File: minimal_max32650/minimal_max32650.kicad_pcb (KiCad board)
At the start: 4 copper layers, 45.2 x 34.3 mm, 38 parts, among them J1 FTSH-105-01-L-DV-K, U1 MAX32650GCE+, U2 ADP225ACPZ-R7

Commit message: development backup
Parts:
- added C28: 4.7 µF, capacitor_footprints:C_0603_1608Metric, F.Cu at (181.7, 75.6)
- added C29: 0.1uF, capacitor_footprints:C_0402_1005Metric, F.Cu at (182.0, 77.0)
- added C30: 1 µF, capacitor_footprints:C_0402_1005Metric, F.Cu at (178.7, 77.0)
- added TP5: TestPoint, test_point_footprints:TestPoint_THTPad_Castelated, F.Cu at (191.0, 73.3)
- added TP6: TestPoint, test_point_footprints:TestPoint_THTPad_Castelated, F.Cu at (189.7, 73.3)
- added U3: MAXQ1065GTC+, analog_devices_footprints:21-0664_TD1233&plus_1C_MXM, F.Cu at (181.0, 79.8)
- moved C26 7.74 mm to (192.9, 78.8)
- moved TP3 7.63 mm to (195.0, 77.7)
- moved TP4 7.63 mm to (195.0, 80.2)
- moved C25 7.43 mm to (190.4, 79.1), turned to 180 degrees
- moved R1 7.25 mm to (188.4, 81.9)
- moved R3 7.25 mm to (192.3, 81.9)
- moved R2 7.25 mm to (188.4, 83.8)
- moved R4 7.25 mm to (192.3, 83.8)
- moved U2 7.25 mm to (190.4, 82.8)
- moved TP1 6.87 mm to (185.8, 77.7)
- moved TP2 6.87 mm to (185.8, 80.2)
- moved C24 6.72 mm to (187.9, 78.8)
- renumbered C26 to C24, C24 to C25, C25 to C26, R2 to R1, R4 to R2, R1 to R3, R3 to R4, TP4 to TP3, TP3 to TP4
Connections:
- U1 pad 1: unconnected-(U1-P2.16-Pad1) -> /MAXQ1065_RDY
- U1 pad 10: unconnected-(U1-P0.22-Pad10) -> /SPI0_SS0
- U1 pad 138: unconnected-(U1-P3.1-Pad138) -> /SPI0_MISO
- U1 pad 141: unconnected-(U1-P3.2-Pad141) -> /SPI0_MOSI
- U1 pad 142: unconnected-(U1-P3.3-Pad142) -> /SPI0_SCK
- U1 pad 2: unconnected-(U1-P0.1-Pad2) -> /MAXQ1065_WDI
- U1 pad 3: unconnected-(U1-P0.2-Pad3) -> /MAXQ1065_PDWN
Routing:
- net /MAXQ1065_PDWN: track 0.00 -> 15.5 mm, vias 0 -> 2
- net /MAXQ1065_WDI: track 0.00 -> 12.9 mm, vias 0 -> 2
- net /MAXQ1065_RDY: track 0.00 -> 11.3 mm, vias 0 -> 2
- net /SPI0_SS0: track 0.00 -> 11.0 mm, vias 0 -> 2
- net /SPI0_MISO: track 0.00 -> 8.00 mm, vias 0 -> 2
- net /SPI0_MOSI: track 0.00 -> 7.77 mm, vias 0 -> 2
- net /SPI0_SCK: track 0.00 -> 6.40 mm, vias 0 -> 2
- net /3V3: track 25.4 -> 30.0 mm, vias 13 -> 15
- net Net-(U3-CEXT): track 0.00 -> 2.42 mm
- net unconnected-(U1-P2.15-Pad144): track 0.00 -> 1.27 mm, vias 0 -> 1
- net unconnected-(U1-P2.14-Pad143): track 0.00 -> 1.27 mm, vias 0 -> 1
- net GND: vias 35 -> 39
- added copper zone on In1.Cu, net /3V3
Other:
- board size 45.2 x 34.3 mm -> 50.3 x 34.3 mm

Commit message: development backup
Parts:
- added C5: 0.1uF, capacitor_footprints:C_0402_1005Metric, F.Cu at (152.3, 84.9)
- added D1: 1.8 V, diode_footprints:LED_GREEN_0402_1005Metric, F.Cu at (179.0, 85.1)
- added D2: 1.8 V, diode_footprints:LED_GREEN_0402_1005Metric, F.Cu at (183.9, 85.1)
- added Q1: 50 V, transistor_footprints:SOT23-3, F.Cu at (181.3, 85.6)
- added Q2: 50 V, transistor_footprints:SOT23-3, F.Cu at (186.2, 85.6)
- added R1: 10k, resistor_footprints:R_0402_1005Metric, F.Cu at (151.0, 76.1)
- added R2: 10k, resistor_footprints:R_0402_1005Metric, F.Cu at (152.2, 76.1)
- added R3: 10k, resistor_footprints:R_0402_1005Metric, F.Cu at (153.4, 76.1)
- added R4: 1 kΩ, resistor_footprints:R_0402_1005Metric, F.Cu at (179.5, 83.4)
- added R5: 1 kΩ, resistor_footprints:R_0402_1005Metric, F.Cu at (184.4, 83.4)
- added U1: ADT75BRMZ, analog_devices_footprints:RM_8_ADI, F.Cu at (151.8, 81.0)
- moved TP5 10.4 mm to (197.9, 79.7), turned to 180 degrees
- moved TP6 10.3 mm to (197.9, 80.9), turned to 180 degrees
- moved TP3 8.00 mm to (193.5, 75.7), turned to 180 degrees
- moved TP4 7.40 mm to (193.5, 84.9), turned to 180 degrees
- moved TP1 6.89 mm to (191.0, 75.7), turned to 180 degrees
- moved TP2 6.18 mm to (191.0, 84.9), turned to 180 degrees
- moved R6 5.59 mm to (187.4, 78.3), turned to 180 degrees
- moved R7 5.23 mm to (187.4, 82.3), turned to 180 degrees
- moved C30 4.59 mm to (192.4, 77.8), turned to 0 degrees
- moved C31 4.01 mm to (192.4, 82.8), turned to 0 degrees
- moved R8 3.63 mm to (189.3, 78.3), turned to 180 degrees
- moved U4 3.17 mm to (188.4, 80.3), turned to 0 degrees
- moved R9 3.04 mm to (189.3, 82.3), turned to 180 degrees
- moved C29 2.04 mm to (192.0, 80.3), turned to 90 degrees
- moved C28 1.48 mm to (190.7, 89.6)
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- renumbered C9 to C10, C10 to C11, C11 to C12, C12 to C13, C13 to C14, C14 to C15, C15 to C16, C16 to C17, C17 to C18, C18 to C19, C30 to C20, C19 to C21, C20 to C22, C21 to C23, C22 to C24, C23 to C25, C28 to C26, C29 to C27, C27 to C28, C25 to C29, C24 to C30, C26 to C31, C5 to C6, C6 to C7, C7 to C8, C8 to C9, R2 to R6, R4 to R7, R1 to R8, R3 to R9, TP2 to TP1, TP4 to TP2, TP1 to TP3, TP3 to TP4, TP6 to TP5, TP5 to TP6, U1 to U2, U2 to U4
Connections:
- U2 pad 143: unconnected-(U1-P2.14-Pad143) -> /LED2
- U2 pad 144: unconnected-(U1-P2.15-Pad144) -> /LED1
- U2 pad 19: unconnected-(U1-P2.17-Pad19) -> /I2C1_SDA
- U2 pad 20: unconnected-(U1-P2.18-Pad20) -> /I2C1_SCL
- U2 pad 39: unconnected-(U1-P1.1-Pad39) -> /ADT75_OS/ALERT
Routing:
- net /I2C1_SCL: track 0.00 -> 17.7 mm, vias 0 -> 2
- net /TCK: track 0.00 -> 16.7 mm, vias 0 -> 2
- net /I2C1_SDA: track 0.00 -> 16.6 mm, vias 0 -> 2
- net /TMS: track 0.00 -> 15.6 mm, vias 0 -> 2
- net /LED1: track 0.00 -> 13.7 mm
- net /UART0_TX: track 0.00 -> 12.5 mm, vias 0 -> 2
- net /RSTN: track 0.00 -> 11.3 mm, vias 0 -> 2
- net /UART0_RX: track 0.00 -> 10.9 mm, vias 0 -> 2
- net /ADT75_OS/ALERT: track 0.00 -> 9.95 mm, vias 0 -> 2
- net /LED2: track 0.00 -> 8.69 mm
- net /3V3: track 30.0 -> 36.3 mm, vias 15 -> 21
- net Net-(D4-Pad2): track 0.00 -> 1.32 mm
- net Net-(D3-Pad2): track 0.00 -> 1.32 mm
- net Net-(Q3-D): track 0.00 -> 1.30 mm
- net Net-(Q2-D): track 0.00 -> 1.30 mm
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- added copper zone on B.Cu, net /1V1
- added copper zone on In1.Cu, net /1V8

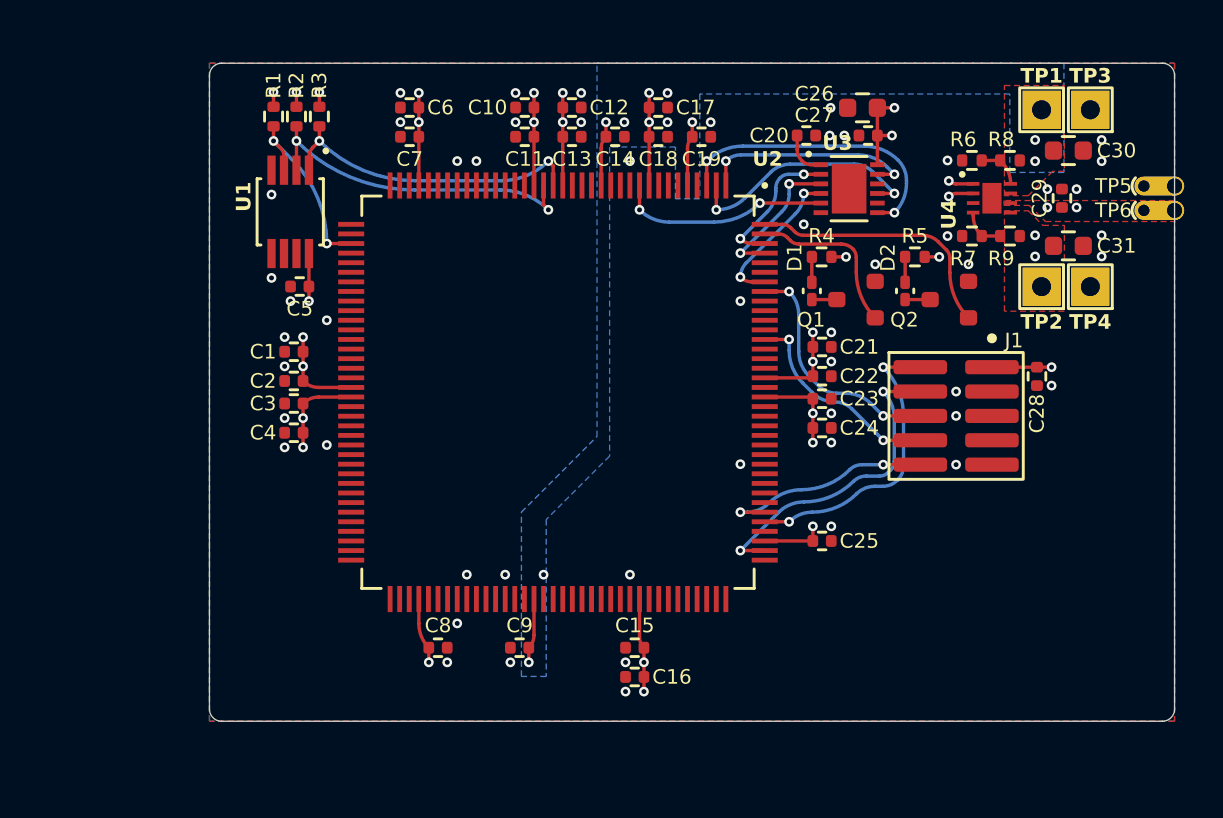
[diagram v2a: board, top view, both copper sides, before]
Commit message: Add SPI interface color mappings to KiCad project
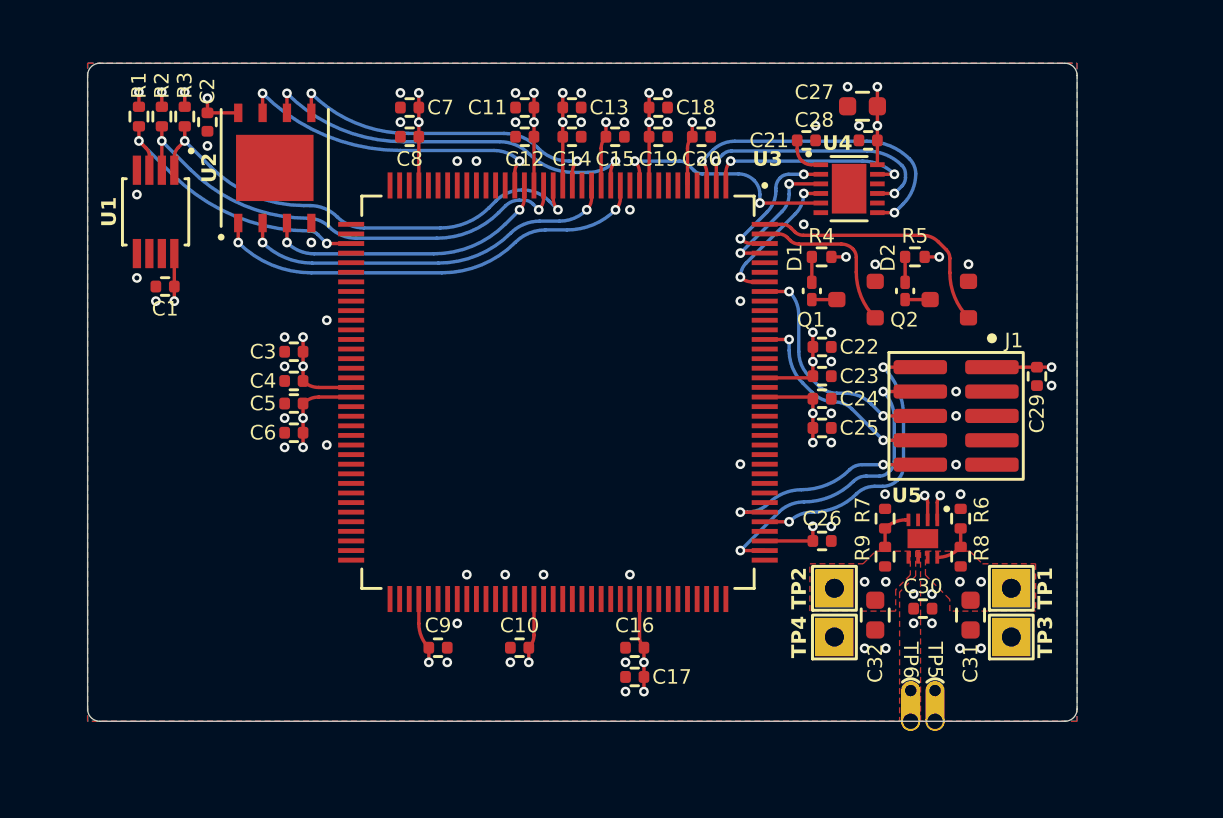
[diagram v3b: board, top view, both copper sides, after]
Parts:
- added C2: 100 nF, capacitor_footprints:C_0402_1005Metric, F.Cu at (147.5, 76.3)
- added U2: MX25U6432FZNI02, macronix_footprints:WSON-8_6X5_MAC, F.Cu at (151.0, 78.7)
- C1: renamed from C5; value 0.1uF -> 100 nF
- C28: renamed from C27; value 0.1uF -> 100 nF
- C29: renamed from C28; value 0.1uF -> 100 nF
- moved TP5 30.6 mm to (185.4, 107.6), turned to 90 degrees
- moved TP6 30.0 mm to (184.2, 107.6), turned to 90 degrees
- moved TP3 27.8 mm to (189.4, 103.2), turned to 90 degrees
- moved TP1 25.0 mm to (189.4, 100.6), turned to 90 degrees
- moved C31 24.7 mm to (187.3, 102.0), turned to -90 degrees
- moved TP4 22.6 mm to (180.2, 103.2), turned to 90 degrees
- moved C30 22.6 mm to (184.8, 101.7), turned to 0 degrees
- moved C32 21.7 mm to (182.3, 102.0), turned to -90 degrees
- moved R8 20.8 mm to (186.8, 99.0), turned to 90 degrees
- moved TP2 19.1 mm to (180.2, 100.6), turned to 90 degrees
- moved R6 18.7 mm to (186.8, 97.0), turned to 90 degrees
- moved U5 18.1 mm to (184.8, 98.1), turned to -90 degrees
- moved R9 17.9 mm to (182.8, 99.0), turned to 90 degrees
- moved R7 15.4 mm to (182.8, 97.0), turned to 90 degrees
- moved C1 7.02 mm to (145.3, 84.9)
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- renumbered C9 to C10, C10 to C11, C11 to C12, C12 to C13, C13 to C14, C14 to C15, C15 to C16, C16 to C17, C17 to C18, C18 to C19, C19 to C20, C20 to C21, C21 to C22, C22 to C23, C23 to C24, C24 to C25, C25 to C26, C26 to C27, C1 to C3, C29 to C30, C30 to C31, C31 to C32, C2 to C4, C3 to C5, C4 to C6, C6 to C7, C7 to C8, C8 to C9, U2 to U3, U3 to U4, U4 to U5
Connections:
- U3 pad 12: unconnected-(U1-P0.7-Pad12) -> /SPIXF_SS0
- U3 pad 13: unconnected-(U1-P0.8-Pad13) -> /SPIXF_SCK
- U3 pad 15: unconnected-(U1-P0.9-Pad15) -> /SPIXF_SDIO1
- U3 pad 17: unconnected-(U1-P0.10-Pad17) -> /SPIXF_SDIO0
- U3 pad 22: unconnected-(U1-P0.11-Pad22) -> /SPIXF_SDIO2
- U3 pad 23: unconnected-(U1-P0.12-Pad23) -> /SPIXF_SDIO3
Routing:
- net /SPIXF_SS0: track 0.00 -> 23.3 mm, vias 0 -> 2
- net /SPIXF_SCK: track 0.00 -> 20.6 mm, vias 0 -> 2
- net /SPIXF_SDIO1: track 0.00 -> 20.2 mm, vias 0 -> 2
- net /SPIXF_SDIO0: track 0.00 -> 17.1 mm, vias 0 -> 2
- net /SPIXF_SDIO3: track 0.00 -> 16.6 mm, vias 0 -> 2
- net /SPIXF_SDIO2: track 0.00 -> 15.3 mm, vias 0 -> 2
- net /I2C1_SDA: track 16.6 -> 25.5 mm
- net /I2C1_SCL: track 17.7 -> 25.5 mm
- net /ADT75_OS/ALERT: track 9.95 -> 15.2 mm
- net /1V8: track 30.6 -> 33.0 mm, vias 14 -> 15
- net /MAXQ1065_PDWN: track 15.5 -> 16.9 mm
- net /SPI0_SS0: track 11.1 -> 12.3 mm
- net /MAXQ1065_WDI: track 13.0 -> 13.9 mm
- net /3V3: track 36.3 -> 35.8 mm
- net GND: vias 56 -> 58
- removed copper zone on B.Cu, net /1V1
- removed copper zone on In1.Cu, net /1V8
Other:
- board size 50.3 x 34.3 mm -> 51.6 x 34.3 mm

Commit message: development backup
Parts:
- added C35: 100 nF, capacitor_footprints:C_0402_1005Metric, F.Cu at (142.7, 90.3)
- added C36: 100 nF, capacitor_footprints:C_0402_1005Metric, F.Cu at (144.2, 90.3)
- added C37: 1 µF, capacitor_footprints:C_0402_1005Metric, F.Cu at (145.7, 90.3)
- added C38: 1 µF, capacitor_footprints:C_0402_1005Metric, F.Cu at (141.4, 95.6)
- added C39: 100 nF, capacitor_footprints:C_0402_1005Metric, F.Cu at (141.4, 94.1)
- added C40: 100 nF, capacitor_footprints:C_0402_1005Metric, F.Cu at (141.4, 92.5)
- added U6: S80KS5122GABHM020, infineon_footprints:PG-BGA-24-801, F.Cu at (146.7, 94.6)
- moved D1 3.43 mm to (182.4, 85.1)
- moved D2 3.43 mm to (187.3, 85.1)
- moved Q1 3.43 mm to (184.7, 85.6)
- moved Q2 3.43 mm to (189.6, 85.6)
- moved R4 3.43 mm to (183.0, 83.4)
- moved R5 3.43 mm to (187.8, 83.4)
- moved R1 1.44 mm to (142.5, 76.1)
- moved R2 1.44 mm to (143.7, 76.1)
- moved R3 1.44 mm to (144.9, 76.1)
- moved U1 1.44 mm to (143.4, 81.0)
- moved U2 1.44 mm to (149.6, 78.7)
- moved C1 1.44 mm to (143.9, 84.9)
- moved C2 1.44 mm to (146.1, 76.3)
- moved R8 1.27 mm to (186.8, 100.3)
- moved R9 1.27 mm to (182.8, 100.3)
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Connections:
- U3 pad 44: unconnected-(U2-P3.0-Pad44) -> /CS1__P3.0
- U3 pad 50: unconnected-(U2-P1.10-Pad50) -> /RESET__P1.10
- U3 pad 52: unconnected-(U2-P1.11-Pad52) -> /CS0__P1.11
- U3 pad 53: unconnected-(U2-P1.12-Pad53) -> /D0__P1.12
- U3 pad 56: unconnected-(U2-P1.13-Pad56) -> /D4__P1.13
- U3 pad 58: unconnected-(U2-P1.15-Pad58) -> /D1__P1.15
- U3 pad 59: unconnected-(U2-P1.16-Pad59) -> /D5__P1.16
- U3 pad 62: unconnected-(U2-P1.19-Pad62) -> /D2__P1.19
- U3 pad 63: unconnected-(U2-P1.18-Pad63) -> /D6__P1.18
- U3 pad 64: unconnected-(U2-~{HYP_CLK}-Pad64) -> /CLK_N
- U3 pad 65: unconnected-(U2-HYP_CLK-Pad65) -> /CLK_P
- U3 pad 66: unconnected-(U2-P1.20-Pad66) -> /D3__P1.20
- U3 pad 67: unconnected-(U2-P1.21-Pad67) -> /D7__P1.21
- U3 pad 68: unconnected-(U2-P1.14-Pad68) -> /RWDS__P1.14
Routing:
- net /D1__P1.15: track 0.00 -> 26.8 mm, vias 0 -> 2
- net /RESET__P1.10: track 0.00 -> 26.1 mm, vias 0 -> 2
- net /CS0__P1.11: track 0.00 -> 23.7 mm, vias 0 -> 2
- net /D0__P1.12: track 0.00 -> 22.3 mm, vias 0 -> 2
- net /D4__P1.13: track 0.00 -> 22.2 mm, vias 0 -> 2
- net /RWDS__P1.14: track 0.00 -> 21.3 mm, vias 0 -> 2
- net /D6__P1.18: track 0.00 -> 21.0 mm, vias 0 -> 2
- net /D7__P1.21: track 0.00 -> 19.5 mm, vias 0 -> 2
- net /D2__P1.19: track 0.00 -> 16.6 mm, vias 0 -> 2
- net /D5__P1.16: track 0.00 -> 14.9 mm, vias 0 -> 2
- net /CLK_N: track 0.00 -> 13.7 mm
- net /D3__P1.20: track 0.00 -> 13.7 mm, vias 0 -> 2
- net /CLK_P: track 0.00 -> 13.6 mm
- net /1V8: track 33.0 -> 45.9 mm, vias 15 -> 22
- net /LED2: track 8.69 -> 12.1 mm
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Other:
- board size 51.6 x 34.3 mm -> 54.1 x 36.8 mm

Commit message: development backup
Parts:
- moved TP1 7.27 mm to (186.4, 97.8), turned to 180 degrees
- moved R5 6.91 mm to (180.2, 100.5), turned to 180 degrees
- moved TP2 6.89 mm to (183.8, 97.8), turned to 180 degrees
- moved TP3 6.72 mm to (186.4, 107.1), turned to 180 degrees
- moved R8 6.68 mm to (180.2, 104.4), turned to 180 degrees
- moved TP4 6.32 mm to (183.8, 107.1), turned to 180 degrees
- moved TP5 6.13 mm to (190.3, 108.8)
- moved TP6 6.13 mm to (191.6, 108.8)
- moved U6 4.73 mm to (181.3, 102.5), turned to 0 degrees
- moved R4 4.58 mm to (182.2, 100.5), turned to 180 degrees
- moved R7 4.21 mm to (182.2, 104.4), turned to 180 degrees
- moved C35 3.91 mm to (185.2, 100.0), turned to 0 degrees
- moved C37 3.35 mm to (185.2, 104.9), turned to 0 degrees
- moved C38 3.35 mm to (186.9, 87.8), turned to 180 degrees
- moved C36 0.53 mm to (184.9, 102.5), turned to 90 degrees
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- renumbered C40 to C1, C4 to C10, C5 to C11, C6 to C12, C7 to C13, C8 to C14, C9 to C15, C10 to C16, C11 to C17, C12 to C18, C13 to C19, C39 to C2, C14 to C20, C15 to C21, C16 to C22, C17 to C23, C18 to C24, C19 to C25, C20 to C26, C21 to C27, C22 to C28, C23 to C29, C38 to C3, C24 to C30, C25 to C31, C26 to C32, C27 to C33, C28 to C34, C31 to C35, C30 to C36, C32 to C37, C29 to C38, C35 to C4, C1 to C5, C36 to C6, C37 to C7, C2 to C8, C3 to C9, R8 to R4, R6 to R5, R4 to R6, R9 to R7, R7 to R8, R5 to R9, TP3 to TP1, TP1 to TP2, TP4 to TP3, TP2 to TP4, TP6 to TP5, TP5 to TP6, U6 to U2, U2 to U3, U3 to U4, U4 to U5, U5 to U6
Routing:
- net /CLK_P: track 13.6 -> 31.0 mm
- net /CLK_N: track 13.7 -> 31.0 mm
- net /D3__P1.20: track 13.7 -> 27.9 mm
- net /D5__P1.16: track 14.9 -> 27.9 mm
- net /D2__P1.19: track 16.6 -> 28.1 mm
- net /D7__P1.21: track 19.5 -> 27.9 mm
- net /D6__P1.18: track 21.0 -> 28.0 mm
- net /RWDS__P1.14: track 21.3 -> 27.9 mm
- net /D4__P1.13: track 22.2 -> 28.1 mm
- net /D1__P1.15: track 26.8 -> 32.5 mm
- net /D0__P1.12: track 22.3 -> 27.9 mm
- net /CS0__P1.11: track 23.7 -> 20.2 mm
- net /RESET__P1.10: track 26.1 -> 22.9 mm
- net /1V8: track 45.9 -> 45.0 mm
- net /TMS: track 15.5 -> 16.3 mm
- added copper zone on In1.Cu, net /1V1
- added copper zone on In1.Cu, net /1V8

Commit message: development backup
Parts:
- added TP1: TestPoint, test_point_footprints:TestPoint_THTPad_Castelated, F.Cu at (141.3, 108.8)
- added TP2: TestPoint, test_point_footprints:TestPoint_THTPad_Castelated, F.Cu at (142.5, 108.8)
- added TP3: TestPoint, test_point_footprints:TestPoint_THTPad_Castelated, F.Cu at (143.8, 108.8)
- added TP4: TestPoint, test_point_footprints:TestPoint_THTPad_Castelated, F.Cu at (145.1, 108.8)
- added TP5: TestPoint, test_point_footprints:TestPoint_THTPad_Castelated, F.Cu at (146.4, 108.8)
- renumbered C36 to C35, C35 to C36, R5 to R4, R8 to R5, R4 to R6, R6 to R8, TP5 to TP10, TP6 to TP11, TP2 to TP6, TP4 to TP7, TP1 to TP8, TP3 to TP9
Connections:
- U4 pad 30: unconnected-(U3-P0.16-Pad30) -> Net-(U4-P0.16)
- U4 pad 31: unconnected-(U3-P0.17-Pad31) -> Net-(U4-P0.17)
- U4 pad 32: unconnected-(U3-P0.18-Pad32) -> Net-(U4-P0.18)
- U4 pad 35: unconnected-(U3-P0.20-Pad35) -> Net-(U4-P0.20)
- U4 pad 36: unconnected-(U3-P0.21-Pad36) -> Net-(U4-P0.21)
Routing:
- net Net-(U4-P0.21): track 0.00 -> 41.6 mm, vias 0 -> 1
- net Net-(U4-P0.20): track 0.00 -> 40.9 mm, vias 0 -> 1
- net Net-(U4-P0.18): track 0.00 -> 40.1 mm, vias 0 -> 1
- net Net-(U4-P0.17): track 0.00 -> 39.3 mm, vias 0 -> 1
- net Net-(U4-P0.16): track 0.00 -> 38.7 mm, vias 0 -> 1
- net /I2C1_SDA: track 26.7 -> 29.1 mm
- net /I2C1_SCL: track 26.8 -> 29.1 mm
- net /SPIXF_SDIO1: track 21.6 -> 23.8 mm
- net /SPIXF_SDIO2: track 16.8 -> 18.9 mm
- net /SPIXF_SS0: track 24.7 -> 26.9 mm
- net /SPIXF_SDIO0: track 18.5 -> 19.9 mm
- net unconnected-(U4-P1.25-Pad72): track 0.00 -> 1.33 mm, vias 0 -> 1
- net unconnected-(U4-P1.23-Pad70): track 0.00 -> 1.33 mm, vias 0 -> 1
- net unconnected-(U4-P1.30-Pad71): track 0.00 -> 1.27 mm, vias 0 -> 1
- net /SPIXF_SCK: track 22.1 -> 23.1 mm
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
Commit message: development backup
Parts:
- added TP1: TestPoint, test_point_footprints:TestPoint_THTPad_Castelated, F.Cu at (145.1, 110.1)
- added TP14: TestPoint, test_point_footprints:TestPoint_THTPad_Castelated, F.Cu at (161.6, 110.1)
- added TP15: TestPoint, test_point_footprints:TestPoint_THTPad_Castelated, F.Cu at (162.9, 110.1)
- added TP16: TestPoint, test_point_footprints:TestPoint_THTPad_Castelated, F.Cu at (164.1, 110.1)
- added TP2: TestPoint, test_point_footprints:TestPoint_THTPad_Castelated, F.Cu at (146.4, 110.1)
- added TP3: TestPoint, test_point_footprints:TestPoint_THTPad_Castelated, F.Cu at (147.6, 110.1)
- added TP4: TestPoint, test_point_footprints:TestPoint_THTPad_Castelated, F.Cu at (148.9, 110.1)
- added TP5: TestPoint, test_point_footprints:TestPoint_THTPad_Castelated, F.Cu at (150.2, 110.1)
- added TP6: TestPoint, test_point_footprints:TestPoint_THTPad_Castelated, F.Cu at (151.4, 110.1)
- added TP7: TestPoint, test_point_footprints:TestPoint_THTPad_Castelated, F.Cu at (152.7, 110.1)
- added TP8: TestPoint, test_point_footprints:TestPoint_THTPad_Castelated, F.Cu at (154.0, 110.1)
- moved TP10 14.0 mm to (156.5, 110.1)
- moved TP11 14.0 mm to (157.8, 110.1)
- moved TP12 14.0 mm to (159.1, 110.1)
- moved TP13 14.0 mm to (160.3, 110.1)
- moved TP9 14.0 mm to (155.2, 110.1)
- moved TP21 1.27 mm to (190.3, 110.1)
- moved TP22 1.27 mm to (191.6, 110.1)
- renumbered TP2 to TP10, TP3 to TP11, TP4 to TP12, TP5 to TP13, TP6 to TP17, TP7 to TP18, TP8 to TP19, TP9 to TP20, TP10 to TP21, TP11 to TP22, TP1 to TP9
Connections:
- U4 pad 100: unconnected-(U4-P0.27-Pad100) -> Net-(U4-P0.27)
- U4 pad 103: unconnected-(U4-P0.26-Pad103) -> Net-(U4-P0.26)
- U4 pad 45: unconnected-(U4-P1.4-Pad45) -> Net-(U4-P1.4)
- U4 pad 46: unconnected-(U4-P1.8-Pad46) -> Net-(U4-P1.8)
- U4 pad 48: unconnected-(U4-P1.9-Pad48) -> Net-(U4-P1.9)
- U4 pad 49: unconnected-(U4-P1.6-Pad49) -> Net-(U4-P1.6)
- U4 pad 70: unconnected-(U4-P1.23-Pad70) -> Net-(U4-P1.23)
- U4 pad 71: unconnected-(U4-P1.30-Pad71) -> Net-(U4-P1.30)
- U4 pad 72: unconnected-(U4-P1.25-Pad72) -> Net-(U4-P1.25)
- U4 pad 75: unconnected-(U4-P1.22-Pad75) -> Net-(U4-P1.22)
- U4 pad 90: unconnected-(U4-P3.9-Pad90) -> Net-(U4-P3.9)
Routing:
- net Net-(U4-P1.6): track 0.00 -> 33.3 mm, vias 0 -> 1
- net Net-(U4-P1.4): track 0.00 -> 32.5 mm, vias 0 -> 1
- net Net-(U4-P1.9): track 0.00 -> 30.6 mm, vias 0 -> 1
- net Net-(U4-P1.8): track 0.00 -> 30.3 mm, vias 0 -> 1
- net Net-(U4-P1.23): track 0.00 -> 18.6 mm, vias 0 -> 1
- net Net-(U4-P1.30): track 0.00 -> 18.0 mm, vias 0 -> 1
- net Net-(U4-P1.25): track 0.00 -> 17.3 mm, vias 0 -> 1
- net Net-(U4-P0.26): track 0.00 -> 15.2 mm, vias 0 -> 1
- net Net-(U4-P0.27): track 0.00 -> 14.7 mm, vias 0 -> 1
- net Net-(U4-P3.9): track 0.00 -> 9.34 mm, vias 0 -> 1
- net Net-(U4-P1.22): track 0.00 -> 8.95 mm, vias 0 -> 1
- net Net-(U4-P0.21): track 41.6 -> 32.8 mm
- net Net-(U4-P0.20): track 40.9 -> 33.1 mm
- net Net-(U4-P0.18): track 40.1 -> 32.6 mm
- net Net-(U4-P0.16): track 38.7 -> 31.8 mm
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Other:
- board size 54.1 x 36.8 mm -> 54.1 x 38.1 mm
